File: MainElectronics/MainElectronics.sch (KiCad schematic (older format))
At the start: 34 parts

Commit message: Annotated Schematic
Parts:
- gave numbers to parts that had none: 34

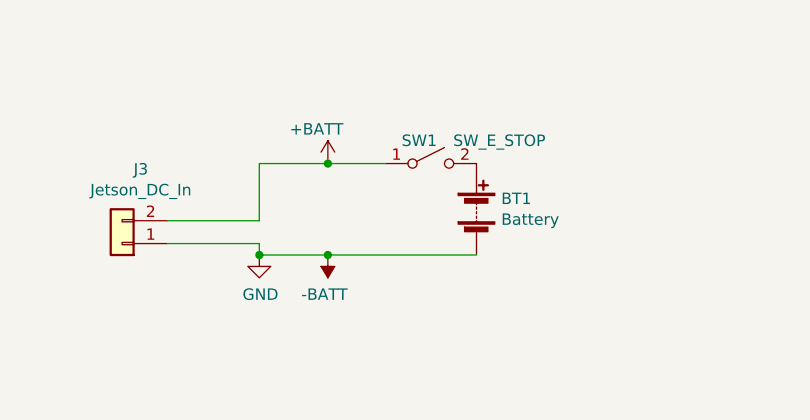
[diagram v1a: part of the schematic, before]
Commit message: Switch has a fancy LED apparently
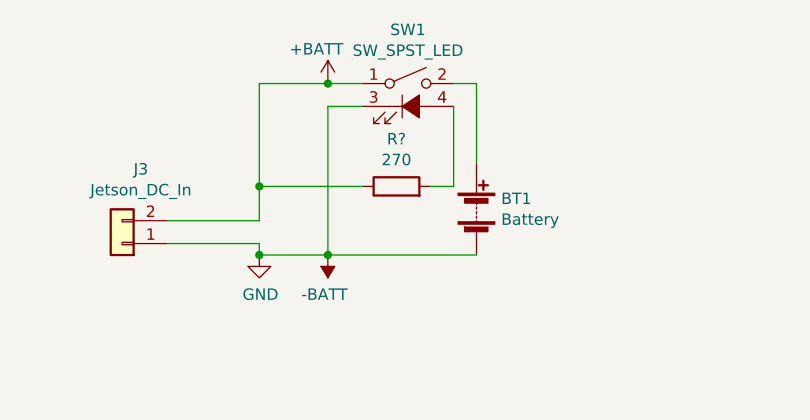
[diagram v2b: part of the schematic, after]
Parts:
- removed SW1: SW_E_STOP, symbol Switch:SW_SPST
- added R?: 270, symbol Device:R
- added SW1: SW_SPST_LED, symbol Switch:SW_SPST_LED
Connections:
- net +BATT: now also R?.1, SW1.1
- net -BATT: now also SW1.3 (K)
- net at BT1.1 (+): now also SW1.2
- new net: R?.2, SW1.4 (A)
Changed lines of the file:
@@
 L power:+BATT #PWR020
 U 1 1 5ED83A12
-P 9550 1250
-F 0 "#PWR020" H 9550 1100 50  0001 C CNN
-F 1 "+BATT" H 9500 1400 50  0000 C CNN
-F 2 "" H 9550 1250 50  0001 C CNN
-F 3 "" H 9550 1250 50  0001 C CNN
-	1    9550 1250
+P 9550 900
+F 0 "#PWR020" H 9550 750 50  0001 C CNN
+F 1 "+BATT" H 9500 1050 50  0000 C CNN
+F 2 "" H 9550 900 50  0001 C CNN
+F 3 "" H 9550 900 50  0001 C CNN
+	1    9550 900
 	1    0    0    -1
 $EndComp
@@
 $EndComp
 $Comp
-L Switch:SW_SPST SW1
-U 1 1 5ED8AA7B
-P 10000 1250
-F 0 "SW1" H 9950 1350 50  0000 C CNN
-F 1 "SW_E_STOP" H 10300 1350 50  0000 C CNN
-F 2 "" H 10000 1250 50  0001 C CNN
-F 3 "~" H 10000 1250 50  0001 C CNN
-	1    10000 1250
-	1    0    0    -1
-$EndComp
-$Comp
 L MainElectronicsLib:RFM95W_Adafruit_Breakout U7
 U 1 1 5ED8CB9C
@@
 $EndComp
 Wire Wire Line
-	9250 1250 9250 1500
-Wire Wire Line
 	9250 1500 8850 1500
 Wire Wire Line
@@
 	9250 1650 9550 1650
 Wire Wire Line
-	9550 1250 9250 1250
-Wire Wire Line
-	9800 1250 9550 1250
-Connection ~ 9550 1250
+	9550 900  9250 900
+Wire Wire Line
+	9700 900  9550 900
+Connection ~ 9550 900
 Wire Wire Line
 	10200 1650 9550 1650
@@
 	1    0    0    -1
 $EndComp
+$Comp
+L Switch:SW_SPST_LED SW1
+U 1 1 5F99F738
+P 9900 1000
+F 0 "SW1" H 9900 1335 50  0000 C CNN
+F 1 "SW_SPST_LED" H 9900 1244 50  0000 C CNN
+F 2 "" H 9900 1300 50  0001 C CNN
+F 3 "~" H 9900 1300 50  0001 C CNN
+	1    9900 1000
+	1    0    0    -1
+$EndComp
+Wire Wire Line
+	10100 900  10200 900
+Wire Wire Line
+	10200 900  10200 1250
+Wire Wire Line
+	9700 1000 9550 1000
+Wire Wire Line
+	9550 1000 9550 1650
+Wire Wire Line
+	9250 900  9250 1350
+$Comp
+L Device:R R?
+U 1 1 5FA3AD30
+P 9850 1350
+F 0 "R?" V 10057 1350 50  0000 C CNN
+F 1 "270" V 9966 1350 50  0000 C CNN
+F 2 "" V 9780 1350 50  0001 C CNN
+F 3 "~" H 9850 1350 50  0001 C CNN
+	1    9850 1350
+	0    -1   -1   0
+$EndComp
+Wire Wire Line
+	10100 1350 10000 1350
+Wire Wire Line
+	10100 1000 10100 1350
+Wire Wire Line
+	9700 1350 9250 1350
+Connection ~ 9250 1350
+Wire Wire Line
+	9250 1350 9250 1500
 $EndSCHEMATC
